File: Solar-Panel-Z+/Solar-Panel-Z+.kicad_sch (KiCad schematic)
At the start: 55 parts, among them J1 FFC2B28-10-G, U1 Value, U2 TSL2561

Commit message: Exported Gerbers
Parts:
- added H1, H2, H3, H4: MountingHole, MountingHole:MountingHole_2.2mm_M2_DIN965, symbol Mechanical:MountingHole
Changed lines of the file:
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@@
     (pin "2")
+  )
+  (symbol (lib_id "Mechanical:MountingHole") (at 204.47 137.795 0) (unit 1)
+    (in_bom yes) (on_board yes) (fields_autoplaced)
+    (property "Reference" "H4" (id 0) (at 207.01 136.9603 0)
+      (effects (font (size 1.27 1.27)) (justify left))
+    )
+    (property "Value" "MountingHole" (id 1) (at 207.01 139.4972 0)
+      (effects (font (size 1.27 1.27)) (justify left))
+    )
+    (property "Footprint" "MountingHole:MountingHole_2.2mm_M2_DIN965" (id 2) (at 204.47 137.795 0)
+      (effects (font (size 1.27 1.27)) hide)
+    )
+    (property "Datasheet" "~" (id 3) (at 204.47 137.795 0)
+      (effects (font (size 1.27 1.27)) hide)
+    )
   )
   (symbol (lib_id "Device:C") (at 186.69 74.676 0) (unit 1)
@@
     (pin "2")
   )
+  (symbol (lib_id "Mechanical:MountingHole") (at 204.343 131.445 0) (unit 1)
+    (in_bom yes) (on_board yes) (fields_autoplaced)
+    (property "Reference" "H3" (id 0) (at 206.883 130.6103 0)
+      (effects (font (size 1.27 1.27)) (justify left))
+    )
+    (property "Value" "MountingHole" (id 1) (at 206.883 133.1472 0)
+      (effects (font (size 1.27 1.27)) (justify left))
+    )
+    (property "Footprint" "MountingHole:MountingHole_2.2mm_M2_DIN965" (id 2) (at 204.343 131.445 0)
+      (effects (font (size 1.27 1.27)) hide)
+    )
+    (property "Datasheet" "~" (id 3) (at 204.343 131.445 0)
+      (effects (font (size 1.27 1.27)) hide)
+    )
+  )
   (symbol (lib_id "power:+3V3") (at 30.226 172.212 0) (unit 1)
     (in_bom yes) (on_board yes)
@@
     (pin "1")
   )
+  (symbol (lib_id "Mechanical:MountingHole") (at 204.343 118.999 0) (unit 1)
+    (in_bom yes) (on_board yes) (fields_autoplaced)
+    (property "Reference" "H1" (id 0) (at 206.883 118.1643 0)
+      (effects (font (size 1.27 1.27)) (justify left))
+    )
+    (property "Value" "MountingHole" (id 1) (at 206.883 120.7012 0)
+      (effects (font (size 1.27 1.27)) (justify left))
+    )
+    (property "Footprint" "MountingHole:MountingHole_2.2mm_M2_DIN965" (id 2) (at 204.343 118.999 0)
+      (effects (font (size 1.27 1.27)) hide)
+    )
+    (property "Datasheet" "~" (id 3) (at 204.343 118.999 0)
+      (effects (font (size 1.27 1.27)) hide)
+    )
+  )
   (symbol (lib_id "Device:R_US") (at 103.632 177.038 180) (unit 1)
     (in_bom yes) (on_board yes)
@@
     (pin "1")
     (pin "2")
+  )
+  (symbol (lib_id "Mechanical:MountingHole") (at 204.343 125.222 0) (unit 1)
+    (in_bom yes) (on_board yes) (fields_autoplaced)
+    (property "Reference" "H2" (id 0) (at 206.883 124.3873 0)
+      (effects (font (size 1.27 1.27)) (justify left))
+    )
+    (property "Value" "MountingHole" (id 1) (at 206.883 126.9242 0)
+      (effects (font (size 1.27 1.27)) (justify left))
+    )
+    (property "Footprint" "MountingHole:MountingHole_2.2mm_M2_DIN965" (id 2) (at 204.343 125.222 0)
+      (effects (font (size 1.27 1.27)) hide)
+    )
+    (property "Datasheet" "~" (id 3) (at 204.343 125.222 0)
+      (effects (font (size 1.27 1.27)) hide)
+    )
   )
   (symbol (lib_id "Device:R_US") (at 150.622 187.198 180) (unit 1)
@@
       (reference "D5") (unit 1) (value "SBDiode") (footprint "solarpanels:SB Diode")
     )
+    (path "/a991215c-d7f8-4d74-b4fb-3a6d0eed12fe"
+      (reference "H1") (unit 1) (value "MountingHole") (footprint "MountingHole:MountingHole_2.2mm_M2_DIN965")
+    )
+    (path "/dd472471-f193-48d5-889c-efd694d3f702"
+      (reference "H2") (unit 1) (value "MountingHole") (footprint "MountingHole:MountingHole_2.2mm_M2_DIN965")
+    )
+    (path "/7c11a07f-525c-45a7-9ad1-361ea90615cc"
+      (reference "H3") (unit 1) (value "MountingHole") (footprint "MountingHole:MountingHole_2.2mm_M2_DIN965")
+    )
+    (path "/141d55e7-f9fa-486e-a08c-0c5785aa9581"
+      (reference "H4") (unit 1) (value "MountingHole") (footprint "MountingHole:MountingHole_2.2mm_M2_DIN965")
+    )
     (path "/2f35205b-6d62-4575-af29-c9ef2a306d2b"

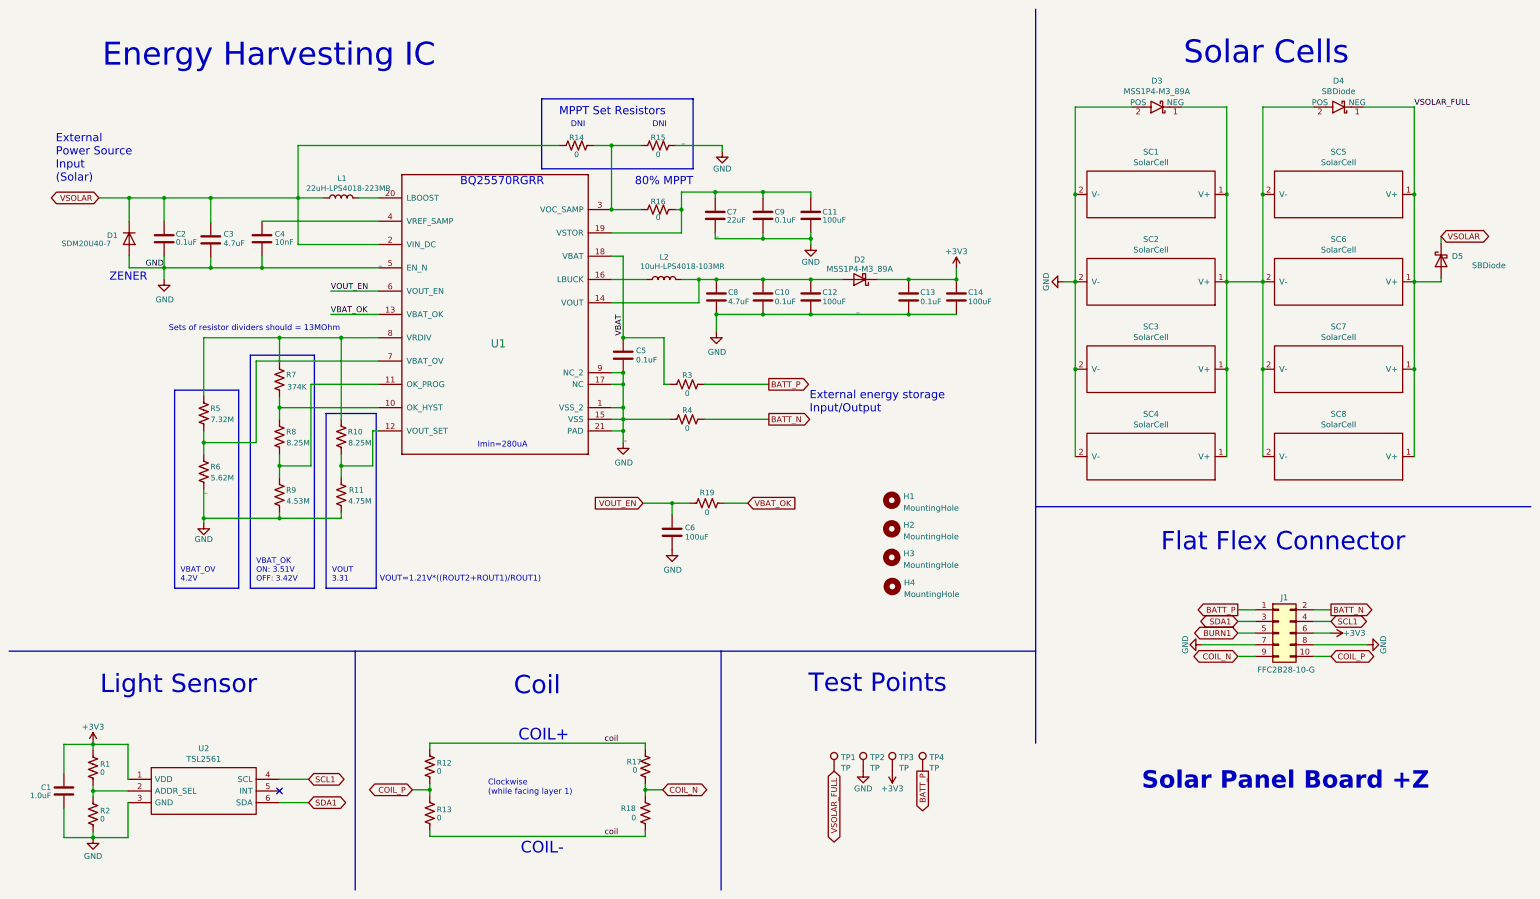
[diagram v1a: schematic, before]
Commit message: Stack architecture schematic updates / fixes
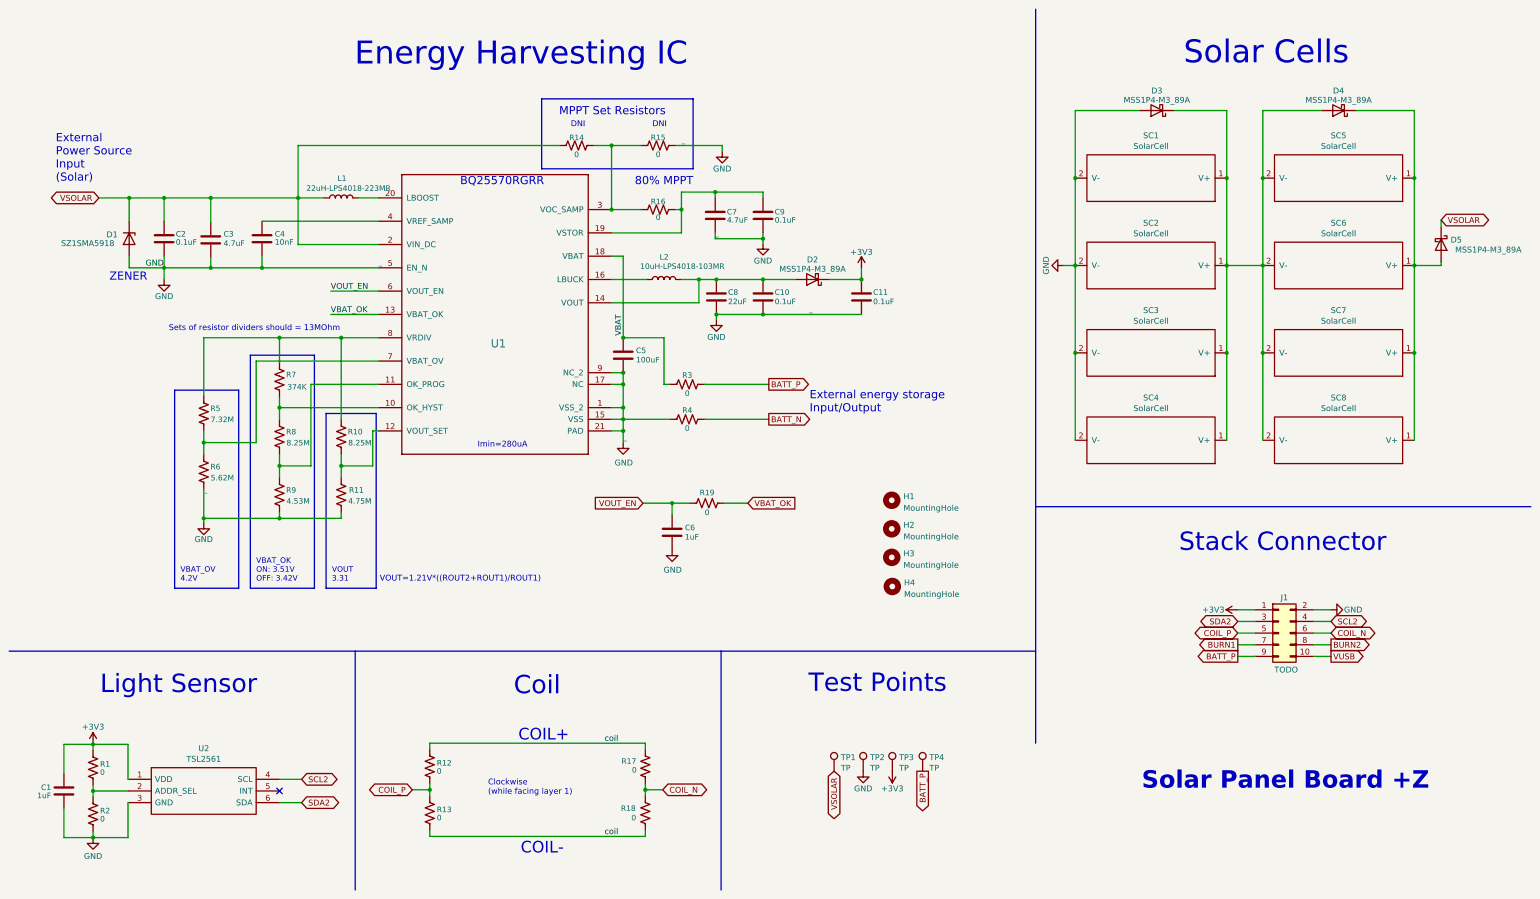
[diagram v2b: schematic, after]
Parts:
- removed C11, C12, C14: 100uF, Capacitor_SMD:C_0603_1608Metric, symbol Device:C
- removed D1: SDM20U40-7, Diode_SMD:D_SOD-523, symbol Device:D
- removed D3: MSS1P4-M3_89A, solarpanels:MICROSMP, symbol solarpanels:SBDiode
- removed D4: SBDiode, solarpanels:SB Diode, symbol solarpanels:SBDiode
- added D1: SZ1SMA5918, Diode_SMD:D_SMA, symbol Diode:Z1SMAxxx
- added D3, D4: MSS1P4-M3_89A, solarpanels:MICROSMP, symbol Device:D_Schottky
- C1: value 1.0uF -> 1uF; footprint Capacitor_SMD:C_0402_1005Metric -> Capacitor_SMD:C_0603_1608Metric
- C10, C2, C3, C4, C9: footprint Capacitor_SMD:C_0402_1005Metric -> Capacitor_SMD:C_0603_1608Metric
- C11: renamed from C13; footprint Capacitor_SMD:C_0402_1005Metric -> Capacitor_SMD:C_0603_1608Metric
- C5: value 0.1uF -> 100uF; footprint Capacitor_SMD:C_0402_1005Metric -> Capacitor_SMD:C_0805_2012Metric
- C6: value 100uF -> 1uF
- C7: value 22uF -> 4.7uF; footprint Capacitor_SMD:C_0402_1005Metric -> Capacitor_SMD:C_0603_1608Metric
- C8: value 4.7uF -> 22uF; footprint Capacitor_SMD:C_0402_1005Metric -> Capacitor_SMD:C_0603_1608Metric
- D5: value SBDiode -> MSS1P4-M3_89A; footprint solarpanels:SB Diode -> solarpanels:MICROSMP
- J1: value FFC2B28-10-G -> TODO
- R1, R10, R11, R12, R13, R14, R15, R16, R17, R18, R19, R2, R3, R4, R5, R6, R7, R8, R9: footprint Resistor_SMD:R_0402_1005Metric -> Resistor_SMD:R_0603_1608Metric
- U1: value Value -> BQ25570RGRR
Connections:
- net +3V3: now also J1.1 (Pin_1); no longer J1.6 (Pin_6)
- net BATT_N: no longer J1.2 (Pin_2)
- net BATT_P: now also J1.9 (Pin_9); no longer J1.1 (Pin_1)
- net BURN1: now also J1.7 (Pin_7); no longer J1.5 (Pin_5)
- net COIL_N: now also J1.6 (Pin_6); no longer J1.9 (Pin_9)
- net COIL_P: now also J1.5 (Pin_5); no longer J1.10 (Pin_10)
- net GND: now also J1.2 (Pin_2), D1.2 (A), D3.2 (A); no longer J1.7 (Pin_7), J1.8 (Pin_8)
- net VSOLAR: now also TP1.1, D1.1 (K)
- net at SC1.1 (V+), SC2.1 (V+), SC3.1 (V+)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: now also D3.1 (K), D4.2 (A)
- net SCL1 renamed SCL2
- net SDA1 renamed SDA2
- net VSOLAR_FULL: no longer names the net of D5.2 (A), SC5.1 (V+), SC6.1 (V+), SC7.1 (V+), SC8.1 (V+)
- net VSOLAR_FULL: now also D4.1 (K); no longer TP1.1
- new net BURN2: J1.8 (Pin_8)
- new net VUSB: J1.10 (Pin_10)
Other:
- note added: "Stack Connector"
- note removed: "Flat Flex Connector"
- moved on the sheet: C11, D2, SC1, SC2, SC3, SC4, SC5, SC6, SC7, SC8

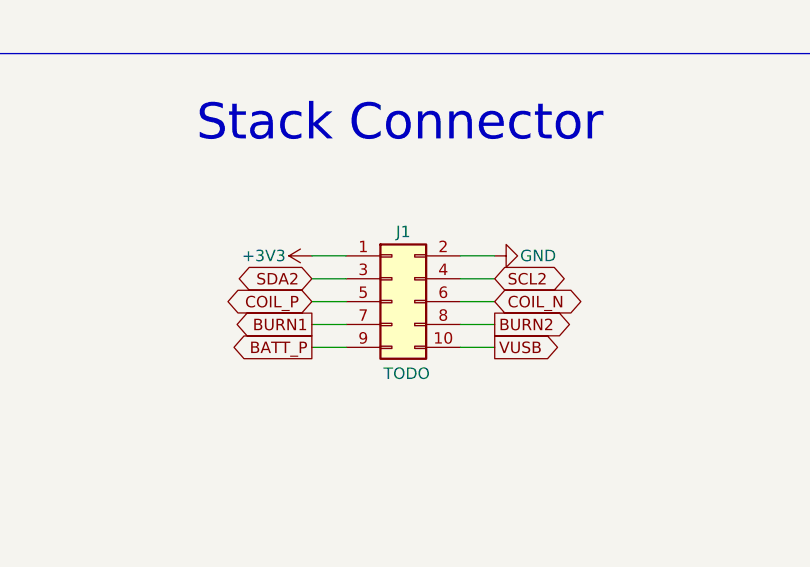
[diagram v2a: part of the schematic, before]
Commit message: Added new edge cuts and connector
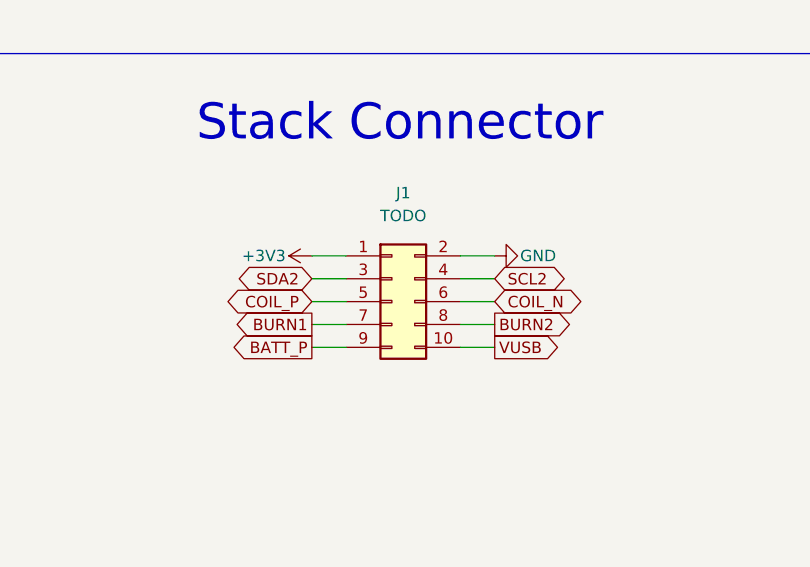
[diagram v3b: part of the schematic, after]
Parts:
- J1: footprint solarpanels:GCT_FFC2B28-10-G -> batteryboard:FTS-105-XX-YY-DV-A
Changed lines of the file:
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@@
   )
   (symbol (lib_id "Connector_Generic:Conn_02x05_Odd_Even") (at 288.671 147.955 0) (unit 1)
-    (in_bom yes) (on_board yes)
-    (property "Reference" "J1" (id 0) (at 289.941 140.208 0))
-    (property "Value" "TODO" (id 1) (at 290.322 155.956 0))
-    (property "Footprint" "solarpanels:GCT_FFC2B28-10-G" (id 2) (at 288.671 147.955 0)
+    (in_bom yes) (on_board yes) (fields_autoplaced)
+    (property "Reference" "J1" (id 0) (at 289.941 135.89 0))
+    (property "Value" "TODO" (id 1) (at 289.941 138.43 0))
+    (property "Footprint" "batteryboard:FTS-105-XX-YY-DV-A" (id 2) (at 288.671 147.955 0)
       (effects (font (size 1.27 1.27)) hide)
     )
@@
     )
     (path "/2f35205b-6d62-4575-af29-c9ef2a306d2b"
-      (reference "J1") (unit 1) (value "TODO") (footprint "solarpanels:GCT_FFC2B28-10-G")
+      (reference "J1") (unit 1) (value "TODO") (footprint "batteryboard:FTS-105-XX-YY-DV-A")
     )
     (path "/910b876e-ca89-4c16-ac14-53a6bc707f92"

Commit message: Added 4 Layer Z+ board
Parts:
- removed R4: 0, Resistor_SMD:R_0603_1608Metric, symbol Device:R_US
- removed SC4, SC7, SC8: SolarCell, solarpanels:KXOB25-05X3F, symbol solarpanels:SolarCell_Small
- added C12, C13: 10nF, Capacitor_SMD:C_0402_1005Metric, symbol Device:C
- added Q1, Q3: BSS138DWQ-7, Package_TO_SOT_SMD:SOT-363_SC-70-6, symbol mainboard:BSS138DWQ-7
- added Q2, Q4: MBT2222ADW1T1, Package_TO_SOT_SMD:SOT-363_SC-70-6, symbol Transistor_BJT:MBT2222ADW1T1
- added R20, R27: 680, Resistor_SMD:R_0402_1005Metric, symbol Device:R_US
- added R21, R28: 100K, Resistor_SMD:R_0402_1005Metric, symbol Device:R_US
- added R22, R23: 0, Resistor_SMD:R_0402_1005Metric, symbol Device:R_US
- added R24, R25, R29, R30: 10K, Resistor_SMD:R_0402_1005Metric, symbol Device:R_US
- added R26, R31: 200K, Resistor_SMD:R_0402_1005Metric, symbol Device:R_US
- added SC6: SolarCell, solarpanels:KXOB25-05X3F, symbol solarpanels:SolarCell_Small
- C1, C10, C11, C2, C3, C4, C6, C7, C8, C9: footprint Capacitor_SMD:C_0603_1608Metric -> Capacitor_SMD:C_0402_1005Metric
- D1: value SZ1SMA5918 -> SZMM5Z5V1T1G; footprint Diode_SMD:D_SMA -> Diode_SMD:D_SOD-523
- H1, H2, H3, H4: footprint MountingHole:MountingHole_2.2mm_M2_DIN965 -> MountingHole:MountingHole_2.2mm_M2_DIN965_Pad; symbol Mechanical:MountingHole -> Mechanical:MountingHole_Pad
- J1: value TODO -> FTS-105-01-L-DV-A
- R1, R10, R11, R12, R13, R14, R15, R16, R17, R18, R19, R2, R3, R5, R6, R7, R8, R9: footprint Resistor_SMD:R_0603_1608Metric -> Resistor_SMD:R_0402_1005Metric
- renumbered SC5 to SC1, SC6 to SC2, SC1 to SC4, SC2 to SC5
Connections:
- net +3V3: now also R21.1, R24.1, R25.1, R28.1, R29.1, R30.1
- net BATT_P: no longer TP4.1
- net BURN1: now also J1.3 (Pin_3); no longer J1.7 (Pin_7)
- net BURN2: now also J1.4 (Pin_4); no longer J1.8 (Pin_8)
- net GND: now also H1.1, H2.1, H3.1, H4.1, C12.2, C13.2, Q1.1 (S2), Q1.4 (S1), Q3.1 (S2), Q3.4 (S1), SC6.2 (V-); no longer SC3.2 (V-)
- net SCL2: now also J1.8 (Pin_8), Q2.1 (E1), Q2.3 (C2), R22.2; no longer J1.4 (Pin_4), U2.4 (SCL)
- net SDA2: now also J1.7 (Pin_7), Q4.1 (E1), Q4.3 (C2), R23.2; no longer J1.3 (Pin_3), U2.6 (SDA)
- net VBAT: now also TP4.1
- net at D3.1 (K), D4.2 (A), SC1.2 (V-)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: now also SC3.2 (V-), SC6.1 (V+); no longer SC3.1 (V+)
- net VSOLAR_FULL: now reaches D4.1 (K), D5.2 (A), SC1.1 (V+), SC2.1 (V+)
- net VSOLAR_FULL: now also SC3.1 (V+)
- new net: Q1.2 (G2), Q1.3 (D2), R21.2
- new net: Q1.6 (D1), Q2.5 (B2), R20.2, R24.2
- new net: C13.1, Q3.5 (G1), R31.2
- new net: Q3.6 (D1), Q4.5 (B2), R27.2, R29.2
- new net: Q3.2 (G2), Q3.3 (D2), R28.2
- new net: Q2.2 (B1), R20.1
- new net: Q4.2 (B1), R27.1
- new net: C12.1, Q1.5 (G1), R26.2
- new net SCL_LS: Q2.4 (E2), Q2.6 (C1), R22.1, R25.2, R26.1, U2.4 (SCL)
- new net SDA_LS: Q4.4 (E2), Q4.6 (C1), R23.1, R30.2, R31.1, U2.6 (SDA)
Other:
- note added: "->"
- note added: "<-"
- note added: "Arrows indicate clockwise (while facing layer 1)"
- note added: "I2C Bus Protection - Light Sensor"
- note added: "Only one resistor per side (COIL_P/COIL_N) should be populated. R12 and R18 should nominally be correct."
- note removed: "Clockwise (while facing layer 1)"
- moved on the sheet: D3, D4, D5, R12, R13, R17, R18, SC1, SC2, SC4, SC5

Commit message: Finish 6 Layer panel versions
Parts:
- removed R31: 200K, Resistor_SMD:R_0402_1005Metric, symbol Device:R_US
- added R4: 0, Resistor_SMD:R_0603_1608Metric, symbol Device:R_US
- C10, C11, C12, C13, C2, C3, C4, C6, C7, C8, C9: footprint Capacitor_SMD:C_0402_1005Metric -> Capacitor_SMD:C_0603_1608Metric
- J1: footprint batteryboard:FTS-105-XX-YY-DV-A -> solarpanels:SAMTEC-FTS-105-01-X-DV-A
- R10, R11, R12, R13, R16, R17, R18, R24, R29, R3, R5, R6, R7, R8, R9: footprint Resistor_SMD:R_0402_1005Metric -> Resistor_SMD:R_0603_1608Metric
- R14, R15: value 0 -> DNI; footprint Resistor_SMD:R_0402_1005Metric -> Resistor_SMD:R_0603_1608Metric
- R19: value 0 -> DNI; footprint Resistor_SMD:R_0402_1005Metric -> Resistor_SMD:R_0603_1608Metric; DNI (none) -> DNI
- R20: value 680 -> DNI; footprint Resistor_SMD:R_0402_1005Metric -> Resistor_SMD:R_0603_1608Metric; DNI (none) -> DNI
- R21: value 100K -> 680; footprint Resistor_SMD:R_0402_1005Metric -> Resistor_SMD:R_0603_1608Metric
- R22: value 0 -> 100K; footprint Resistor_SMD:R_0402_1005Metric -> Resistor_SMD:R_0603_1608Metric; DNI DNI -> (none)
- R23: value 0 -> 10K; footprint Resistor_SMD:R_0402_1005Metric -> Resistor_SMD:R_0603_1608Metric; DNI DNI -> (none)
- R25, R30: value 10K -> 200K; footprint Resistor_SMD:R_0402_1005Metric -> Resistor_SMD:R_0603_1608Metric
- R26: value 200K -> 680; footprint Resistor_SMD:R_0402_1005Metric -> Resistor_SMD:R_0603_1608Metric
- R27: value 680 -> 100K; footprint Resistor_SMD:R_0402_1005Metric -> Resistor_SMD:R_0603_1608Metric
- R28: value 100K -> 10K; footprint Resistor_SMD:R_0402_1005Metric -> Resistor_SMD:R_0603_1608Metric
- SC1, SC2, SC3, SC4, SC5, SC6: value SolarCell -> SolarCell_Small
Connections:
- net BURN2 is gone; now on net GND: J1.4 (Pin_4)
- net VUSB is gone; now on net BATT_P: J1.10 (Pin_10)
- net +3V3: now also R22.1, R23.1, R27.1; no longer R21.1, R25.1, R30.1
- net SCL_LS: now also R19.1, R24.2, R25.1; no longer R22.1, R25.2, R26.1
- net SDA_LS: now also R20.1, R29.2, R30.1; no longer R23.1, R30.2
- net VBAT_OK: now also R4.1; no longer R19.1
- net VOUT_EN: now also R4.2; no longer R19.2
- net at Q1.2 (G2), Q1.3 (D2): now also R22.2; no longer R21.2
- net at Q1.6 (D1), Q2.5 (B2): now also R21.2, R23.2; no longer R20.2, R24.2
- net at C13.1, Q3.5 (G1): now also R30.2
- net at Q3.6 (D1), Q4.5 (B2): now also R26.2, R28.2; no longer R27.2, R29.2
- net at Q3.2 (G2), Q3.3 (D2): now also R27.2; no longer R28.2
- net at Q2.2 (B1): now also R21.1; no longer R20.1
- net at Q4.2 (B1): now also R26.1; no longer R27.1
- net at C12.1, Q1.5 (G1): now also R25.2; no longer R26.2
- net SCL2 renamed SCL
- net SCL: now also R19.2; no longer R22.2
- net SDA2 renamed SDA
- net SDA: now also R20.2; no longer R23.2
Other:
- note added: "Solar Panel Board Z+"
- note removed: "Solar Panel Board +Z"
